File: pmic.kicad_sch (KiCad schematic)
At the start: 43 parts, among them J401 EMI shield frame, U401 STPMIC1DPQR

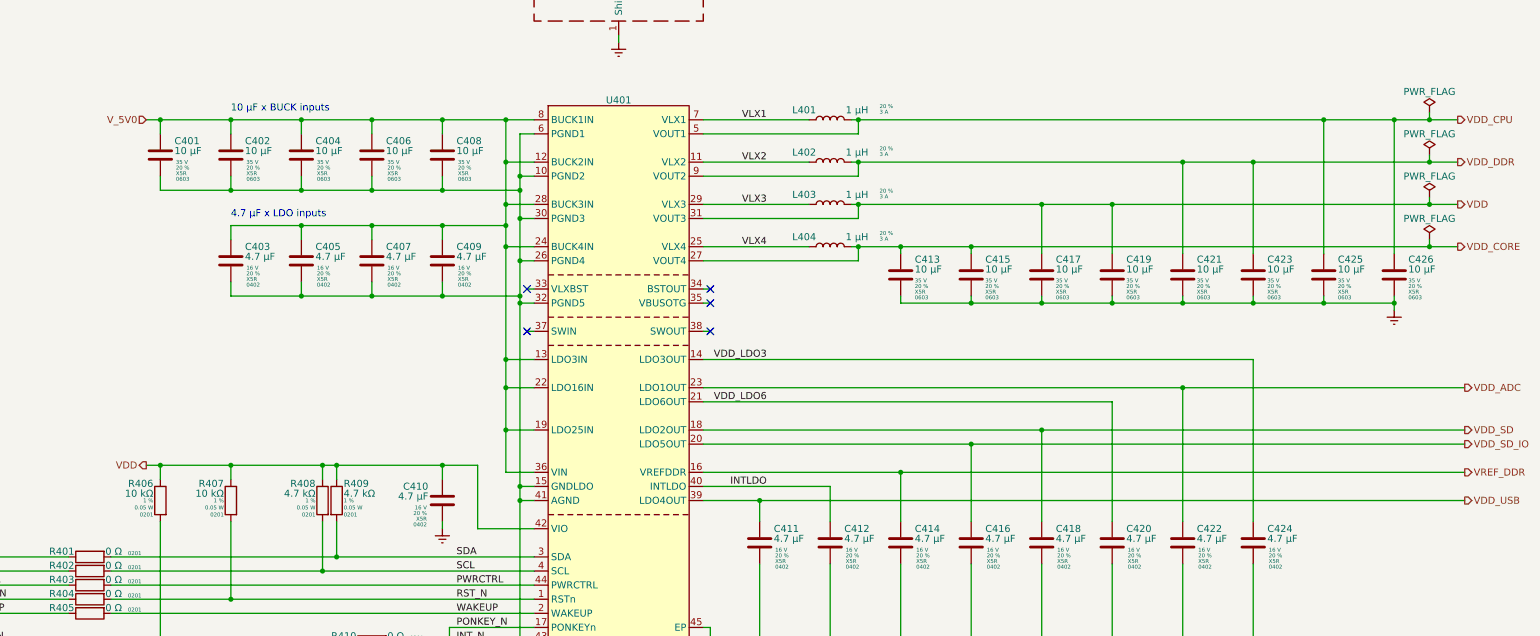
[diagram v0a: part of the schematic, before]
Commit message: PMIC: Remove redundant decoupling
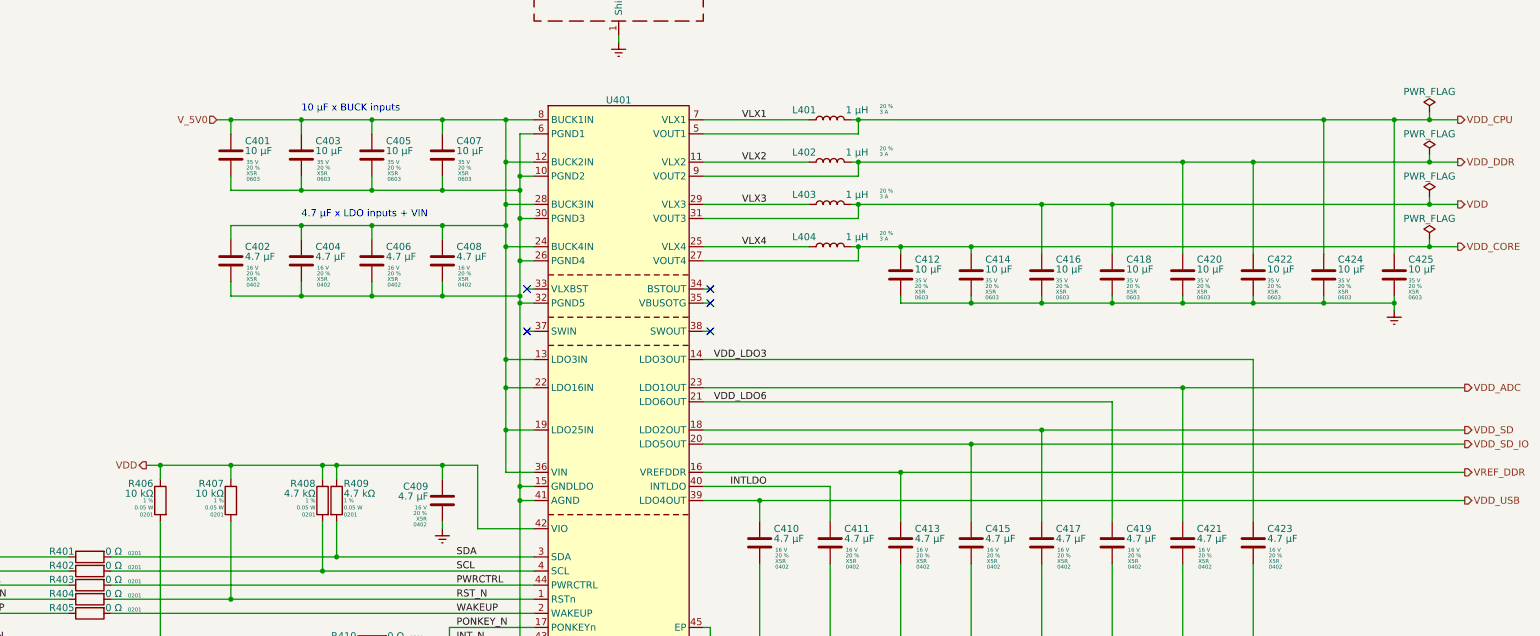
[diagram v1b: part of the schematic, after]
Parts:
- removed C408: 10 µF, Capacitor_SMD:C_0603_1608Metric, symbol Device:C
- renumbered C403 to C402, C402 to C403, C405 to C404, C404 to C405, C407 to C406, C406 to C407, C409 to C408, C410 to C409, C411 to C410, C412 to C411, C413 to C412, C414 to C413, C415 to C414, C416 to C415, C417 to C416, C418 to C417, C419 to C418, C420 to C419, C421 to C420, C422 to C421, C423 to C422, C424 to C423, C425 to C424, C426 to C425
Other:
- note added: "4.7 µF x LDO inputs + VIN"
- note removed: "4.7 µF x LDO inputs"
- moved on the sheet: C401, C403, C405, C407

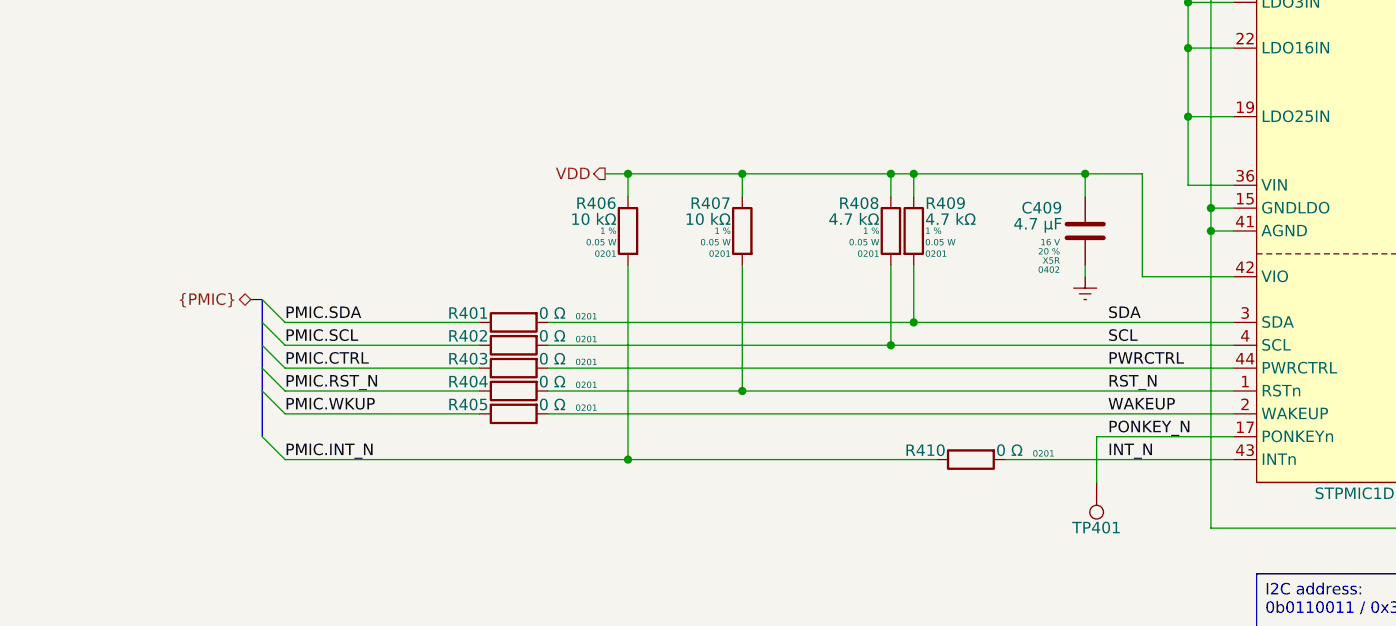
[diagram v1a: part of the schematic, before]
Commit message: Reorganize schematics
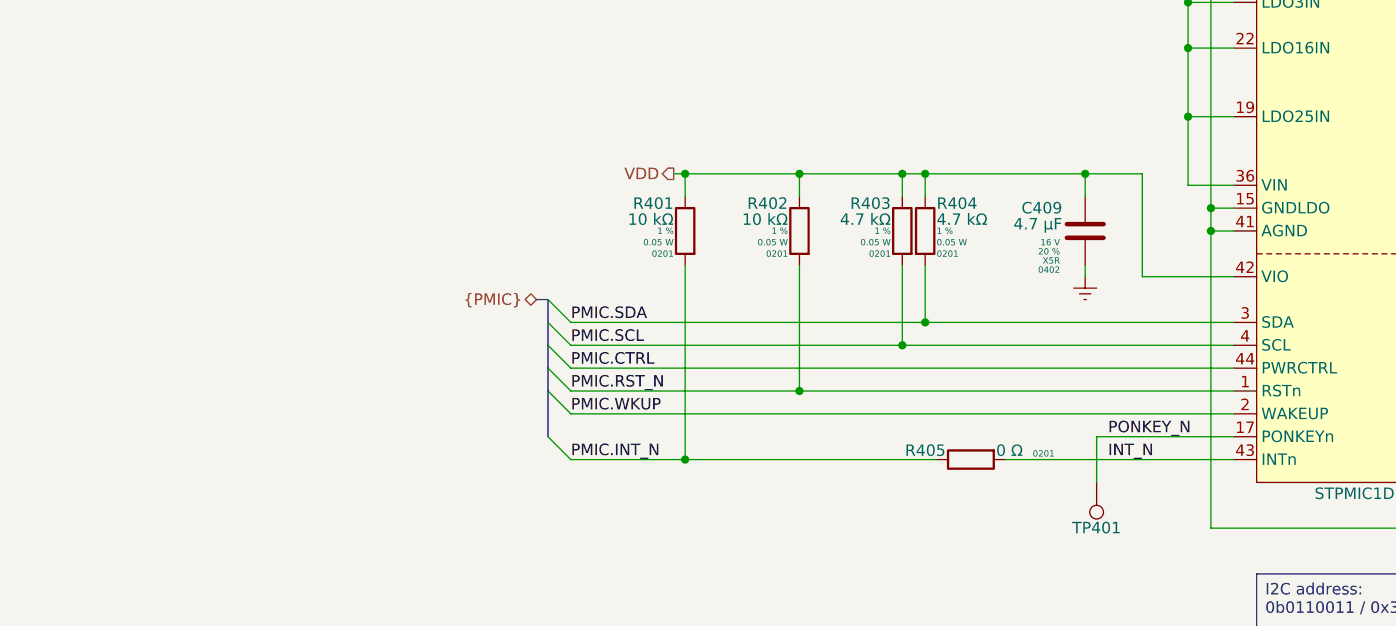
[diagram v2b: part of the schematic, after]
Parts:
- removed R401, R402, R403, R404, R405: 0 Ω, perfect_footprints:R_0201_0603Metric, symbol Device:R
- renumbered R406 to R401, R407 to R402, R408 to R403, R409 to R404, R410 to R405
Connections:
- net PWRCTRL is gone; now on net PMIC.CTRL: U401.44 (PWRCTRL)
- net RST_N is gone; now on net PMIC.RST_N: R402.2, U401.1 (RSTn)
- net SCL is gone; now on net PMIC.SCL: R403.2, U401.4 (SCL)
- net SDA is gone; now on net PMIC.SDA: R404.2, U401.3 (SDA)
- net WAKEUP is gone; now on net PMIC.WKUP: U401.2 (WAKEUP)
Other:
- moved on the sheet: R401, R402, R403, R404

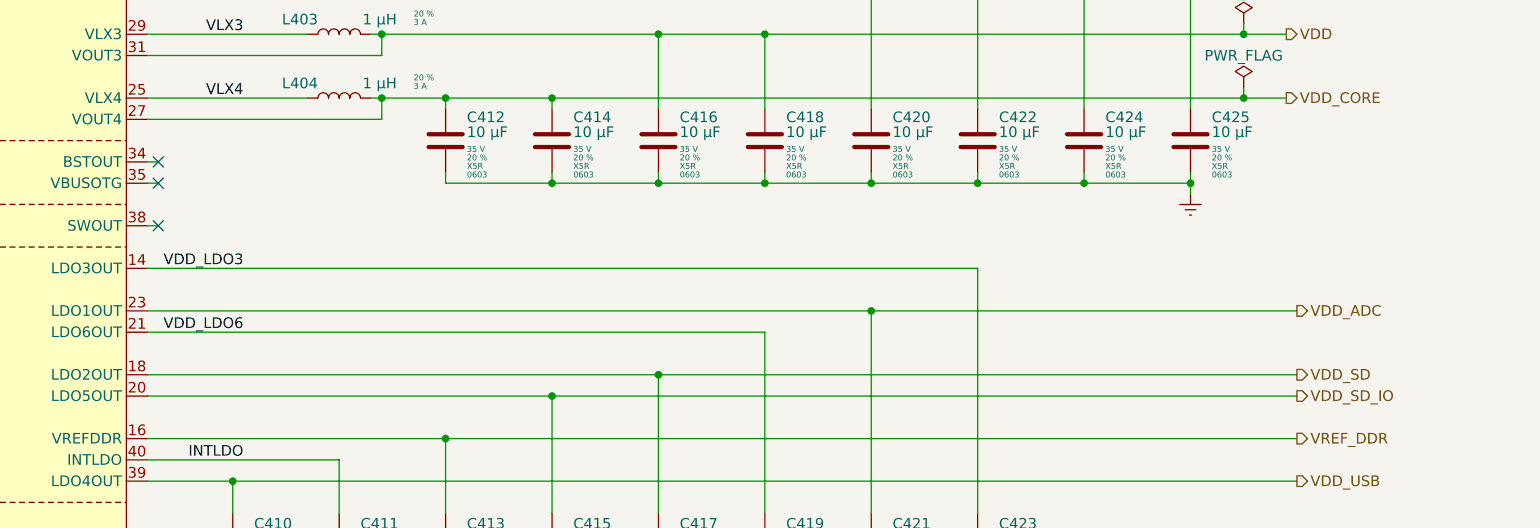
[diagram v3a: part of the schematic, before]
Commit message: DDR: Replace series termination with parallel
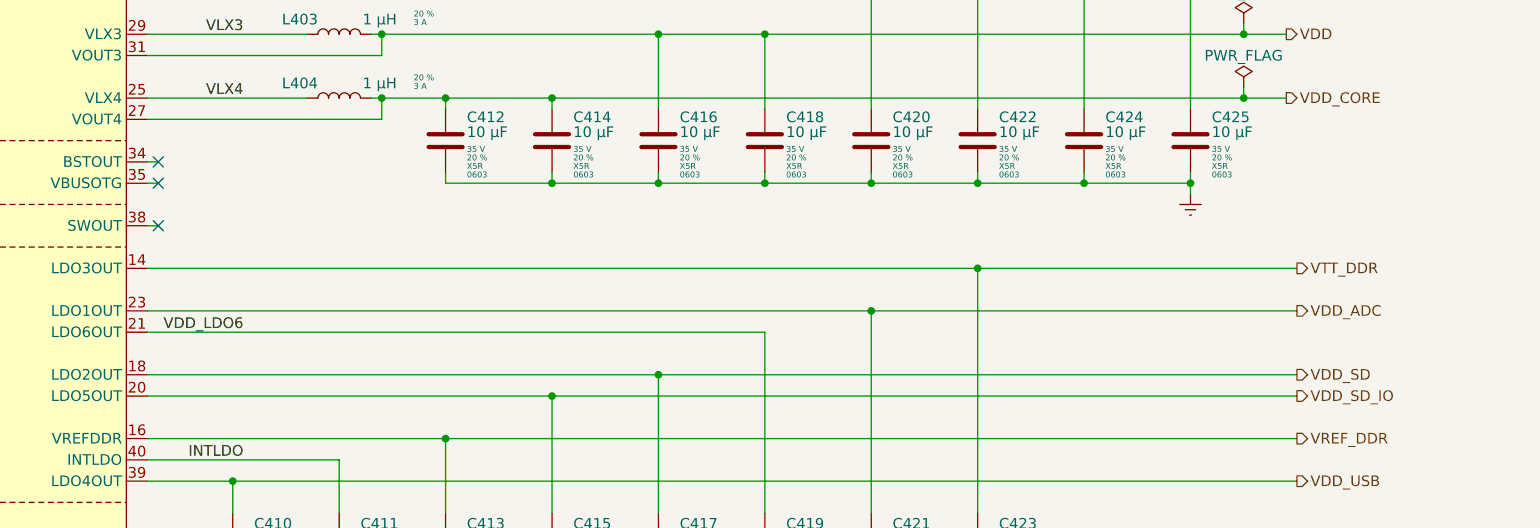
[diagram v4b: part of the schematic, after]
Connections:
- net VDD_LDO3 renamed VTT_DDR
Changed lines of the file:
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@@
+	)
+	(junction
+		(at 292.1 157.48)
+		(diameter 0)
+		(color 0 0 0 0)
 	)
 	(junction
@@
 	(wire
 		(pts
+			(xy 292.1 157.48) (xy 330.2 157.48)
+		)
+		(stroke
+			(width 0)
+			(type default)
+		)
+	)
+	(wire
+		(pts
 			(xy 254 129.54) (xy 254 138.43)
 		)
@@
 			(width 0)
 			(type default)
-		)
-	)
-	(label "VDD_LDO3"
-		(at 204.47 157.48 180)
-		(effects
-			(font
-				(size 1.27 1.27)
-			)
-			(justify right bottom)
 		)
 	)
@@
 		(effects
 			(font
+				(size 1.27 1.27)
+			)
+			(justify left)
+		)
+	)
+	(hierarchical_label "VTT_DDR"
+		(shape output)
+		(at 330.2 157.48 0)
+		(effects
+			(font

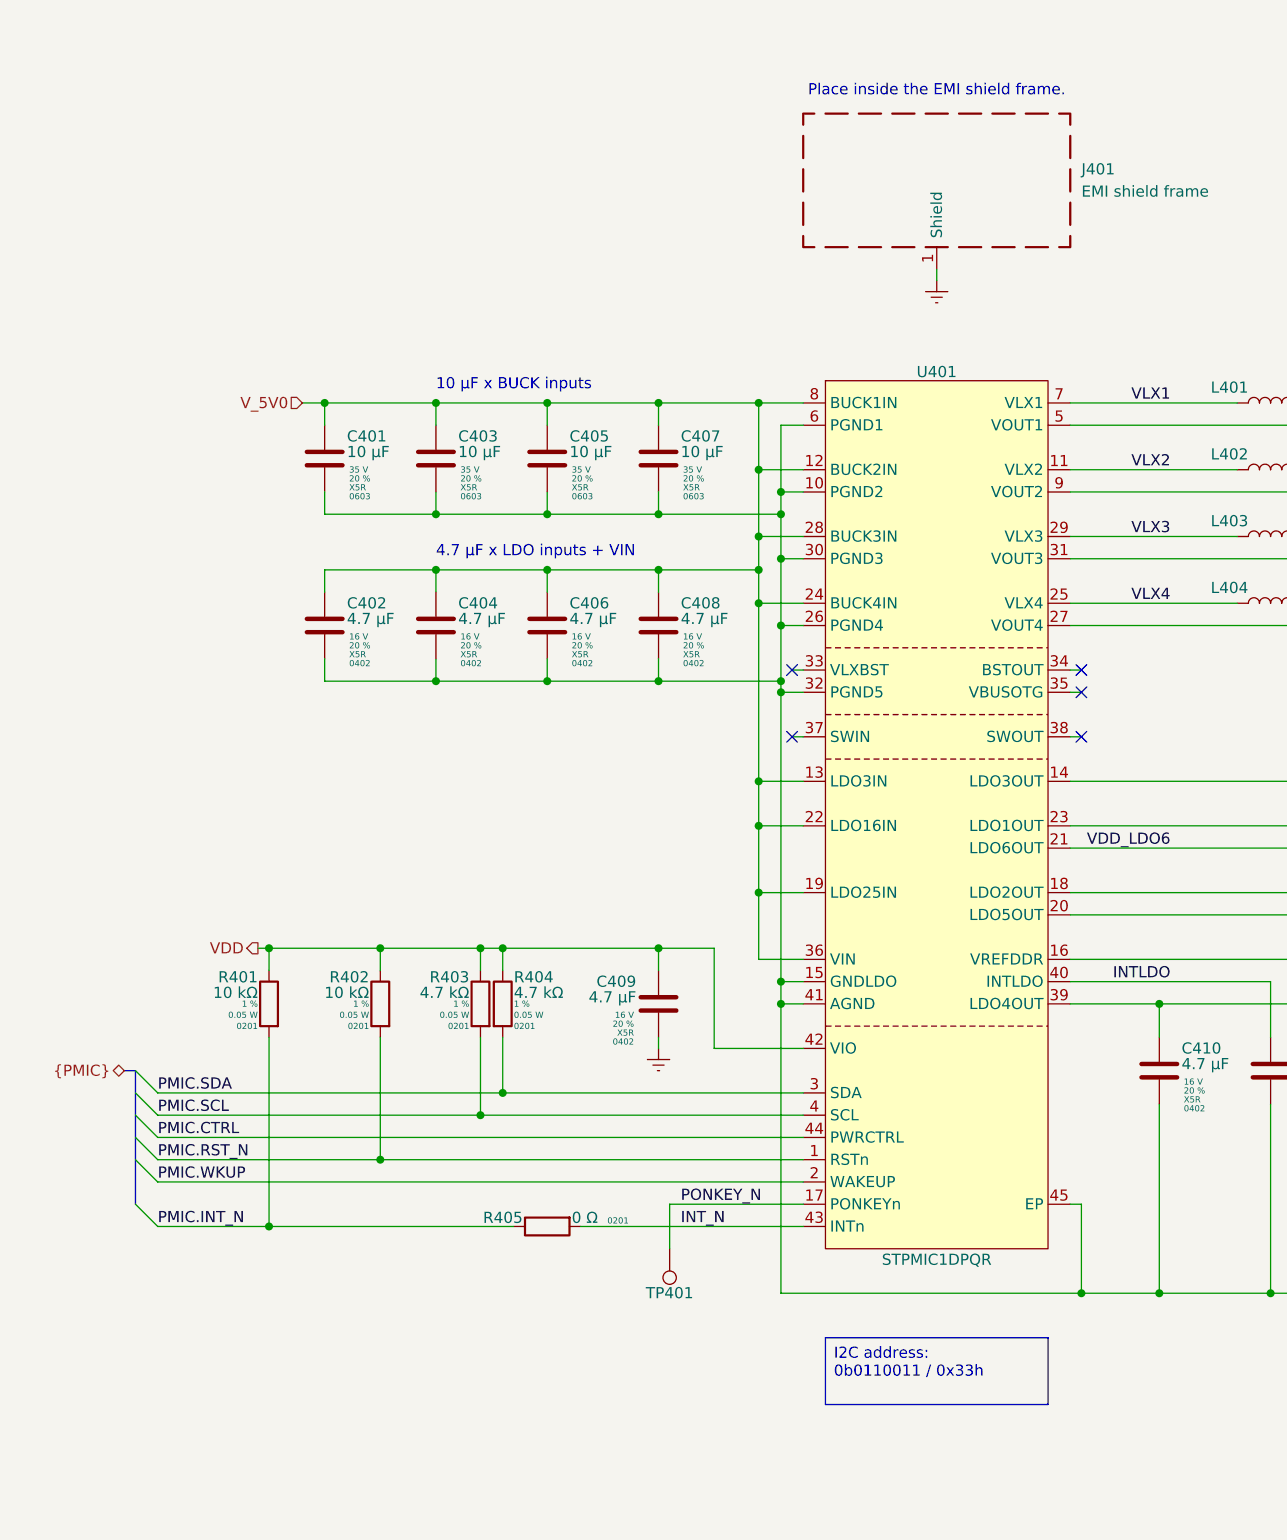
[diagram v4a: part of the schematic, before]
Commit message: Add I2C header to PMIC and power LDO3 from VDD_DDR
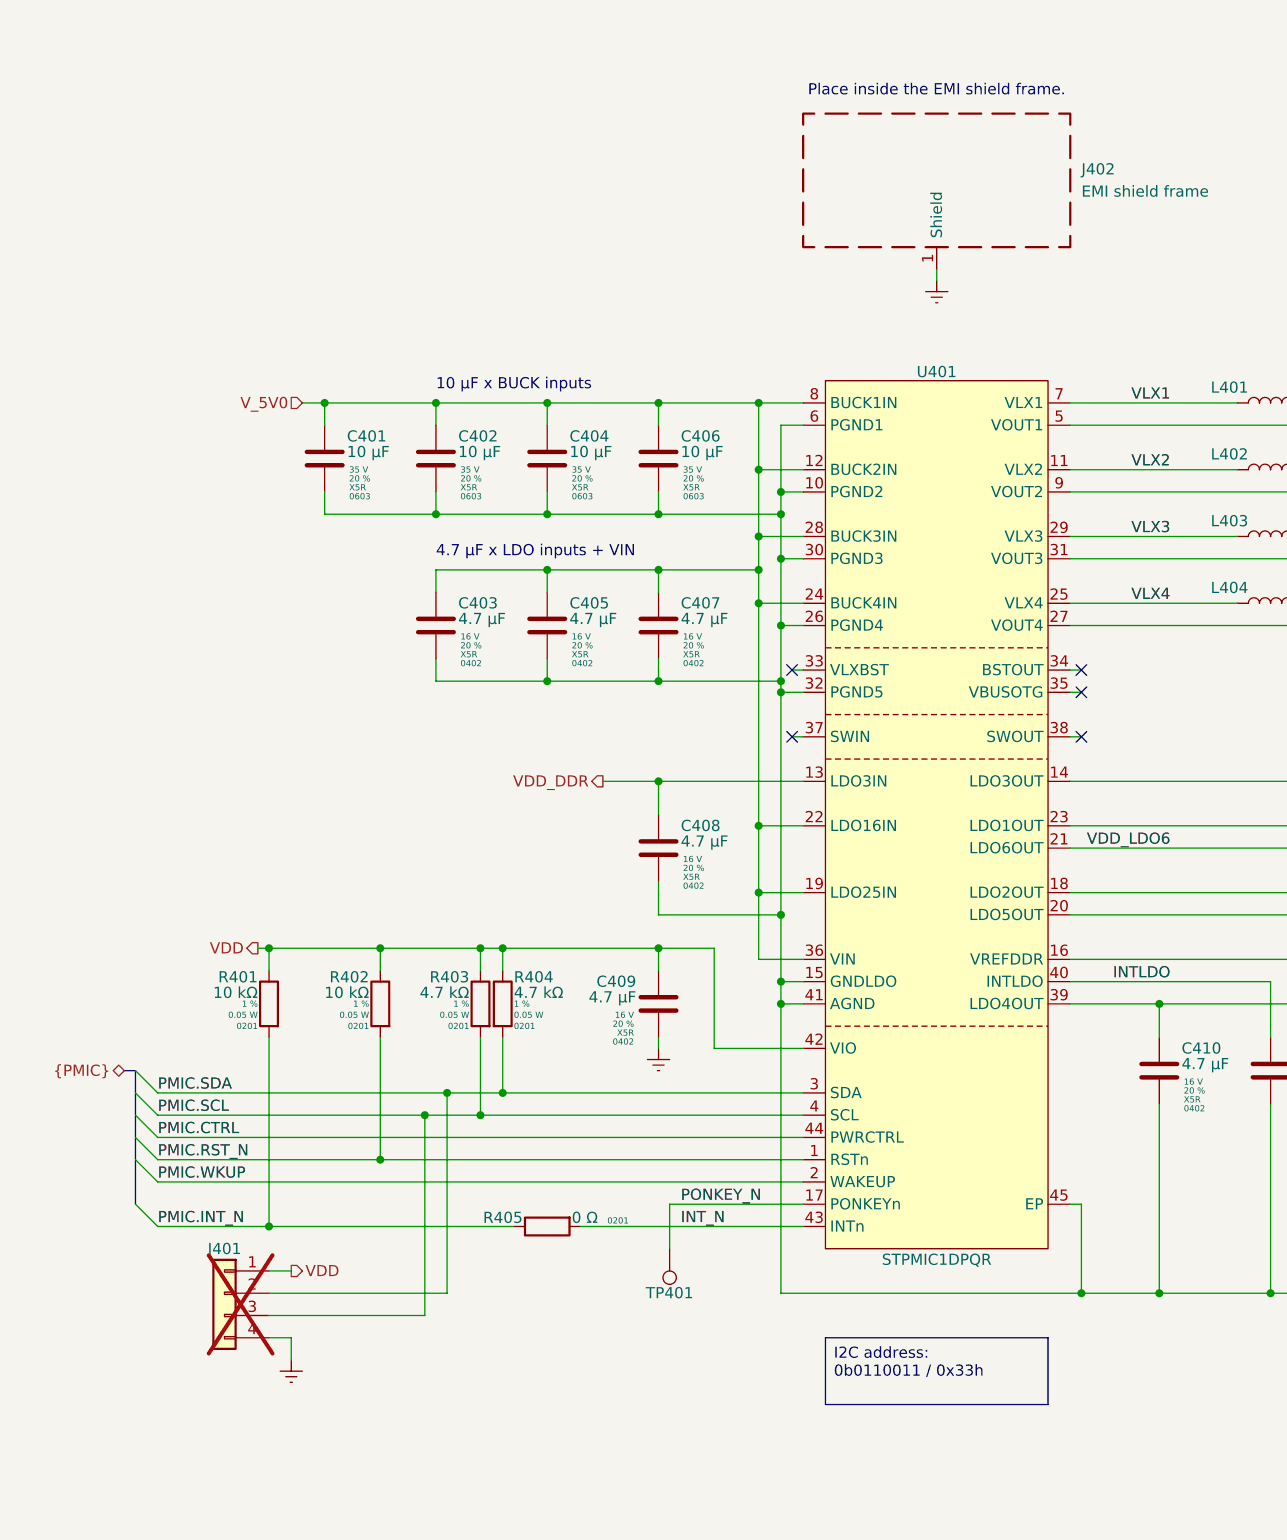
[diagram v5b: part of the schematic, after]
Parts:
- added J401: Conn_01x04, Connector_PinHeader_2.54mm:PinHeader_1x04_P2.54mm_Vertical, symbol Connector_Generic:Conn_01x04
- renumbered C403 to C402, C404 to C403, C405 to C404, C406 to C405, C407 to C406, C408 to C407, C402 to C408, J401 to J402
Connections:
- net GND: now also J401.4 (Pin_4)
- net PMIC.SCL: now also J401.3 (Pin_3)
- net PMIC.SDA: now also J401.2 (Pin_2)
- net VDD: now also J401.1 (Pin_1)
- net VDD_DDR: now also C408.1, U401.13 (LDO3IN)
- net V_5V0: no longer C408.1, U401.13 (LDO3IN)
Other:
- moved on the sheet: C408
